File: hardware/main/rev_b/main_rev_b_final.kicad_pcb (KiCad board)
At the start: 4 copper layers, 130 x 86 mm, 165 parts, among them J1 USB-C USB2, J10 SWD, J2 ESC_CAN_POWER, J30 GNSS_UFL, J40 915MHz_ANT, Q30 2N7002, U1 USBLC6-2SC6, U10 RP2354B, U2 TLV62569DBVR, U20 ICM-42688-P, U21 LSM6DSO32TR, U22 LPS22DFTR, U3 TLV75528PDBVR, U30 LG77LICMD, U4 TLV75533PDBVR, U40 CC1121RHBR, U41 CC1190RGVR, U50 TCAN3413DR, U51 MCP2518FD-H/QBB, Y1 12MHz ABM8-272-T3, Y40 32MHz NT2016SA-32M-TEE3017A, Y50 40MHz ABM8G

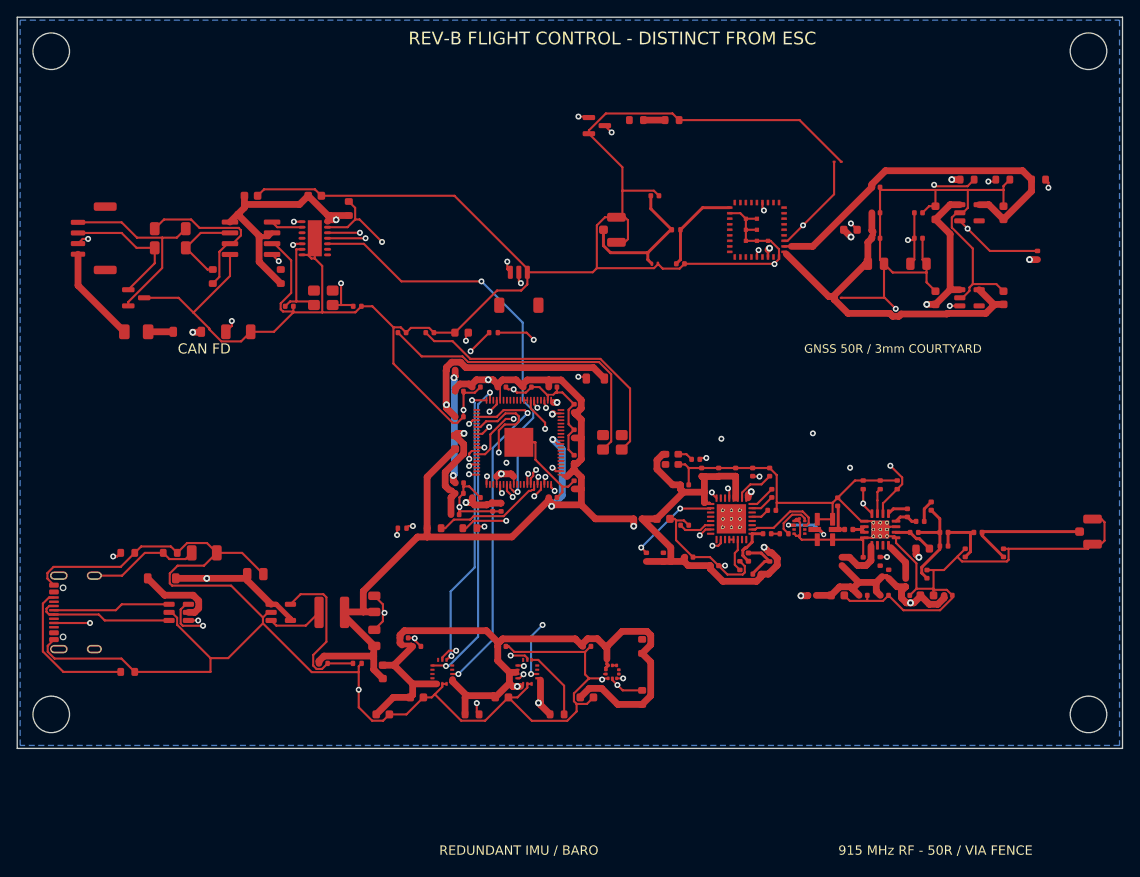
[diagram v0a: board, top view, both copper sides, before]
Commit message: Add Main Rev B ESC interfaces
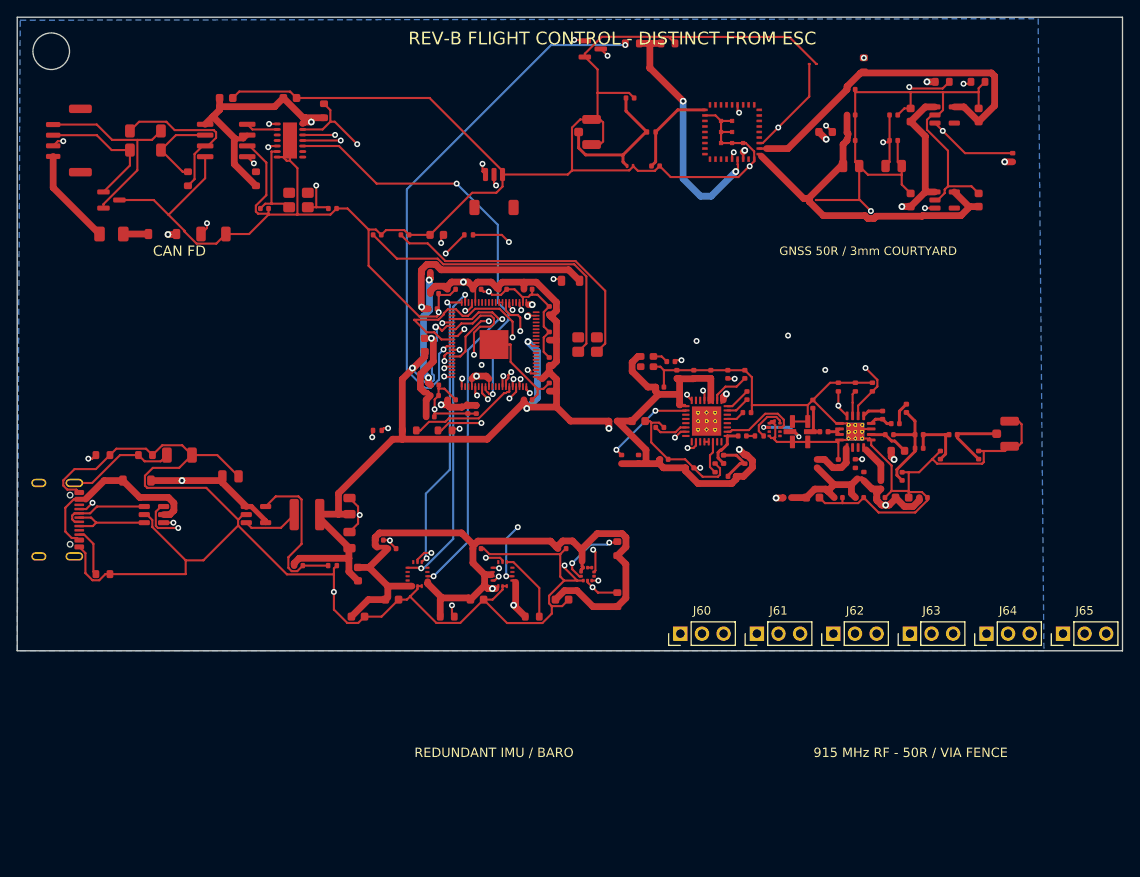
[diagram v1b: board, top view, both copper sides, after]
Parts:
- removed H2, H3, H4: M4, MountingHole_4.3mm_M4
- added J60: ESC_PWM_1, PinHeader_1x03_P2.54mm_Vertical, F.Cu at (78.0, 72.5)
- added J61: ESC_PWM_2, PinHeader_1x03_P2.54mm_Vertical, F.Cu at (87.0, 72.5)
- added J62: ESC_PWM_3, PinHeader_1x03_P2.54mm_Vertical, F.Cu at (96.0, 72.5)
- added J63: ESC_PWM_4, PinHeader_1x03_P2.54mm_Vertical, F.Cu at (105.0, 72.5)
- added J64: ESC_PWM_5, PinHeader_1x03_P2.54mm_Vertical, F.Cu at (114.0, 72.5)
- added J65: ESC_PWM_6, PinHeader_1x03_P2.54mm_Vertical, F.Cu at (123.0, 72.5)
- moved R34 24.6 mm to (99.6, 5.60), turned to 90 degrees
- moved J40 15.1 mm to (116.2, 49.0)
- moved C11 13.1 mm to (48.9, 34.3)
- moved FB1 12.0 mm to (47.9, 38.5)
- moved R33 11.9 mm to (113.0, 7.60)
- moved C1 11.9 mm to (25.1, 54.0)
- moved C10 11.9 mm to (49.1, 32.5)
- moved C100 11.9 mm to (73.1, 47.5)
- moved C101 11.9 mm to (75.6, 43.5)
- moved C102 11.9 mm to (77.6, 42.0)
- moved C103 11.9 mm to (79.6, 42.0)
- moved C104 11.9 mm to (81.6, 42.0)
- moved C105 11.9 mm to (76.1, 52.0)
- moved C106 11.9 mm to (79.1, 53.0)
- moved C110 11.9 mm to (93.6, 56.5)
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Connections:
- U10 pad 43: unconnected-(U10-GPIO34-Pad43) -> /RP2354B MCU/PWM_ESC1
- U10 pad 44: unconnected-(U10-GPIO35-Pad44) -> /RP2354B MCU/PWM_ESC2
- U10 pad 45: unconnected-(U10-GPIO36-Pad45) -> /RP2354B MCU/PWM_ESC3
- U10 pad 46: unconnected-(U10-GPIO37-Pad46) -> /RP2354B MCU/PWM_ESC4
- U10 pad 47: unconnected-(U10-GPIO38-Pad47) -> /RP2354B MCU/PWM_ESC5
- U10 pad 48: unconnected-(U10-GPIO39-Pad48) -> /RP2354B MCU/PWM_ESC6
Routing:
- net /GNSS_TX: track 0.00 -> 65.1 mm, vias 0 -> 2
- net /BARO_DRDY: track 0.00 -> 52.4 mm, vias 0 -> 2
- net /GNSS/GNSS_UART_RX_2V8: track 2.55 -> 29.9 mm, vias 0 -> 2
- net /GNSS/GNSS_RESET_OD: track 64.5 -> 42.8 mm
- net /Power and USB/CHASSIS: track 32.5 -> 12.8 mm
- net /GND: track 821.9 -> 805.9 mm
- net /3V3: track 285.5 -> 299.0 mm, vias 9 -> 11
- net /Power and USB/USB_VBUS: track 9.39 -> 21.6 mm
- net /Power and USB/USB_CC2: track 17.4 -> 5.80 mm
- net /BARO_SCL: track 0.22 -> 8.68 mm, vias 0 -> 2
- net /915 MHz RF/ANT_915: track 15.4 -> 8.60 mm
- net /Power and USB/USB_DP_CONN: track 16.2 -> 10.1 mm
- net /LSM_INT1: track 46.5 -> 52.1 mm
- net /GNSS_RESET_N: track 99.7 -> 95.3 mm
- net /Power and USB/USB_CC1: track 14.3 -> 9.93 mm
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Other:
- board size 130 x 86 mm -> 130 x 74.5 mm
- board text added: "PCB Edge"

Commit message: main: route CAN_5V/CAN_GND chains to J60-J65 headers and J2/F1/R3; 56->47 unconnected
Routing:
- net /CAN_5V: track 11.4 -> 94.4 mm
- net /CAN_GND: track 23.9 -> 62.0 mm
